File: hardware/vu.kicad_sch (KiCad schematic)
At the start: 3 parts, among them U4 LM3915N

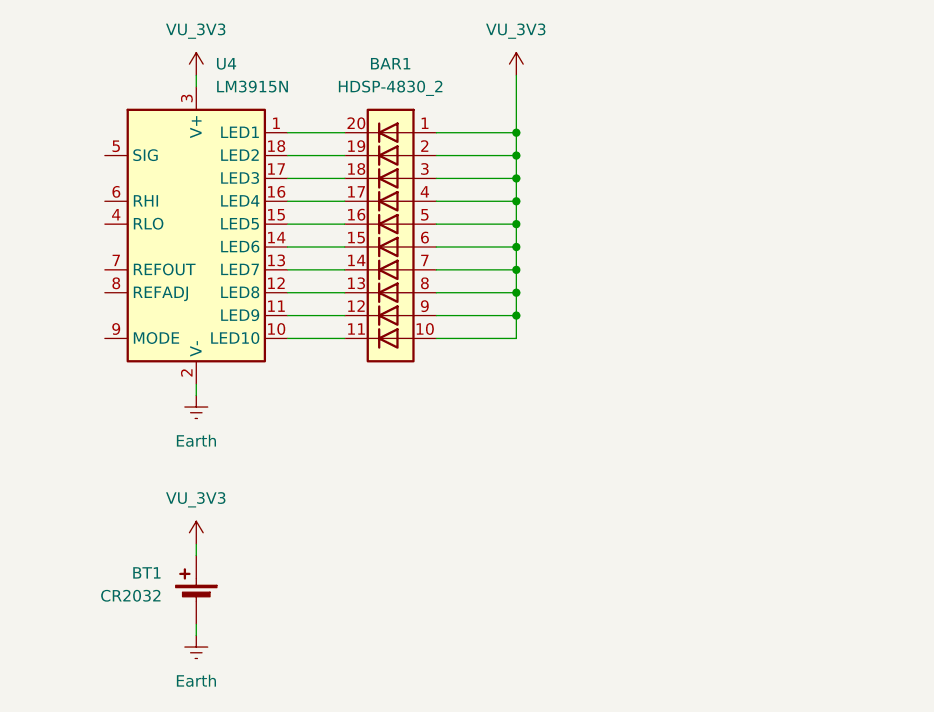
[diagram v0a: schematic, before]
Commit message: done first 3 pcbs
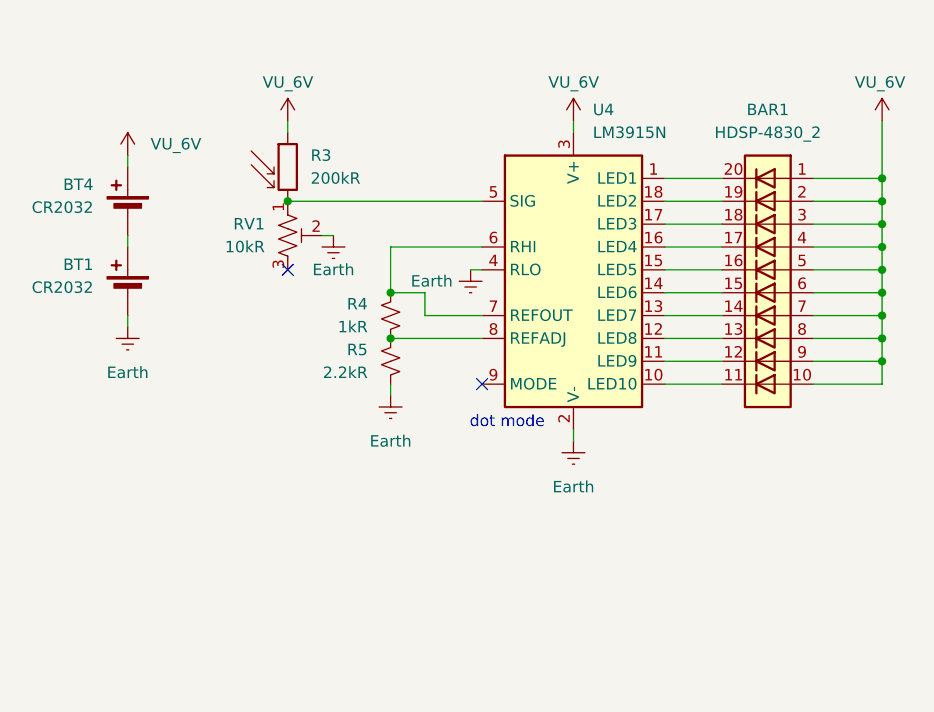
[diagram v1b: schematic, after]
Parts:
- added BT4: CR2032, Battery:BatteryHolder_Keystone_103_1x20mm, symbol Device:Battery_Cell
- added R3: 200kR, OptoDevice:R_LDR_5.1x4.3mm_P3.4mm_Vertical, symbol Device:R_Photo
- added R4: 1kR, Resistor_THT:R_Axial_DIN0207_L6.3mm_D2.5mm_P7.62mm_Horizontal, symbol Device:R_Small_US
- added R5: 2.2kR, Resistor_THT:R_Axial_DIN0207_L6.3mm_D2.5mm_P7.62mm_Horizontal, symbol Device:R_Small_US
- added RV1: 10kR, Potentiometer_THT:Potentiometer_ACP_CA9-H5_Horizontal, symbol Device:R_Potentiometer_Trim_US
- BAR1: footprint Display:HDSP-4830 -> Display:HDSP-48xx; DIGIKEY (none) -> 160-1067-ND
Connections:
- net Earth: now also U4.4 (RLO), R5.1, RV1.2
- net at U4.5 (SIG): now also R3.2, RV1.1
- net at U4.6 (RHI): now also U4.7 (REFOUT), R4.2
- net at U4.8 (REFADJ): now also R4.1, R5.2
- net VU_3V3 renamed VU_6V
- net VU_6V: now also BT4.1 (+), R3.1; no longer BT1.1 (+)
- new net: BT1.1 (+), BT4.2 (-)
- no-connect marks 0 -> 2
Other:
- note added: "dot mode"
- moved on the sheet: BAR1, BT1, U4

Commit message: prod stuff
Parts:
- BT1, BT4: LCSC (none) -> C70376
- R4: footprint Resistor_THT:R_Axial_DIN0207_L6.3mm_D2.5mm_P7.62mm_Horizontal -> Resistor_THT:R_Axial_DIN0204_L3.6mm_D1.6mm_P5.08mm_Horizontal; LCSC (none) -> C2896955
- R5: footprint Resistor_THT:R_Axial_DIN0207_L6.3mm_D2.5mm_P7.62mm_Horizontal -> Resistor_THT:R_Axial_DIN0204_L3.6mm_D1.6mm_P5.08mm_Horizontal; LCSC (none) -> C2896997
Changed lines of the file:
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@@
+			)
+		)
+		(property "LCSC" "C70376"
+			(at 132.08 91.44 0)
+			(hide yes)
+			(show_name no)
+			(do_not_autoplace no)
+			(effects
+				(font
+					(size 1.27 1.27)
+				)
 			)
 		)
@@
 			)
 		)
-		(property "Footprint" "Resistor_THT:R_Axial_DIN0207_L6.3mm_D2.5mm_P7.62mm_Horizontal"
+		(property "Footprint" "Resistor_THT:R_Axial_DIN0204_L3.6mm_D1.6mm_P5.08mm_Horizontal"
 			(at 161.29 107.95 0)
 			(hide yes)
@@
 		)
 		(property "Description" "Resistor, small US symbol"
+			(at 161.29 107.95 0)
+			(hide yes)
+			(show_name no)
+			(do_not_autoplace no)
+			(effects
+				(font
+					(size 1.27 1.27)
+				)
+			)
+		)
+		(property "LCSC" "C2896997"
 			(at 161.29 107.95 0)
 			(hide yes)
@@
 			)
 		)
-		(property "Footprint" "Resistor_THT:R_Axial_DIN0207_L6.3mm_D2.5mm_P7.62mm_Horizontal"
+		(property "Footprint" "Resistor_THT:R_Axial_DIN0204_L3.6mm_D1.6mm_P5.08mm_Horizontal"
 			(at 161.29 102.87 0)
 			(hide yes)
@@
 		)
 		(property "Description" "Resistor, small US symbol"
+			(at 161.29 102.87 0)
+			(hide yes)
+			(show_name no)
+			(do_not_autoplace no)
+			(effects
+				(font
+					(size 1.27 1.27)
+				)
+			)
+		)
+		(property "LCSC" "C2896955"
 			(at 161.29 102.87 0)
 			(hide yes)
@@
 			(at 132.08 100.33 0)
 			(hide yes)
+			(show_name no)
+			(do_not_autoplace no)
+			(effects
+				(font
+					(size 1.27 1.27)
+				)
+			)
+		)
+		(property "LCSC" "C70376"
+			(at 132.08 100.33 0)
+			(hide yes)
